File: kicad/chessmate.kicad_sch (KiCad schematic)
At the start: 37 parts, among them J1 SPKR, Q1 2N2222, Q2 2N2222, Q3 2N2222, Q4 2N2222, Q5 2N2222, SW1 F6, SW10 ENTER, SW11 CLEAR, SW12 H8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

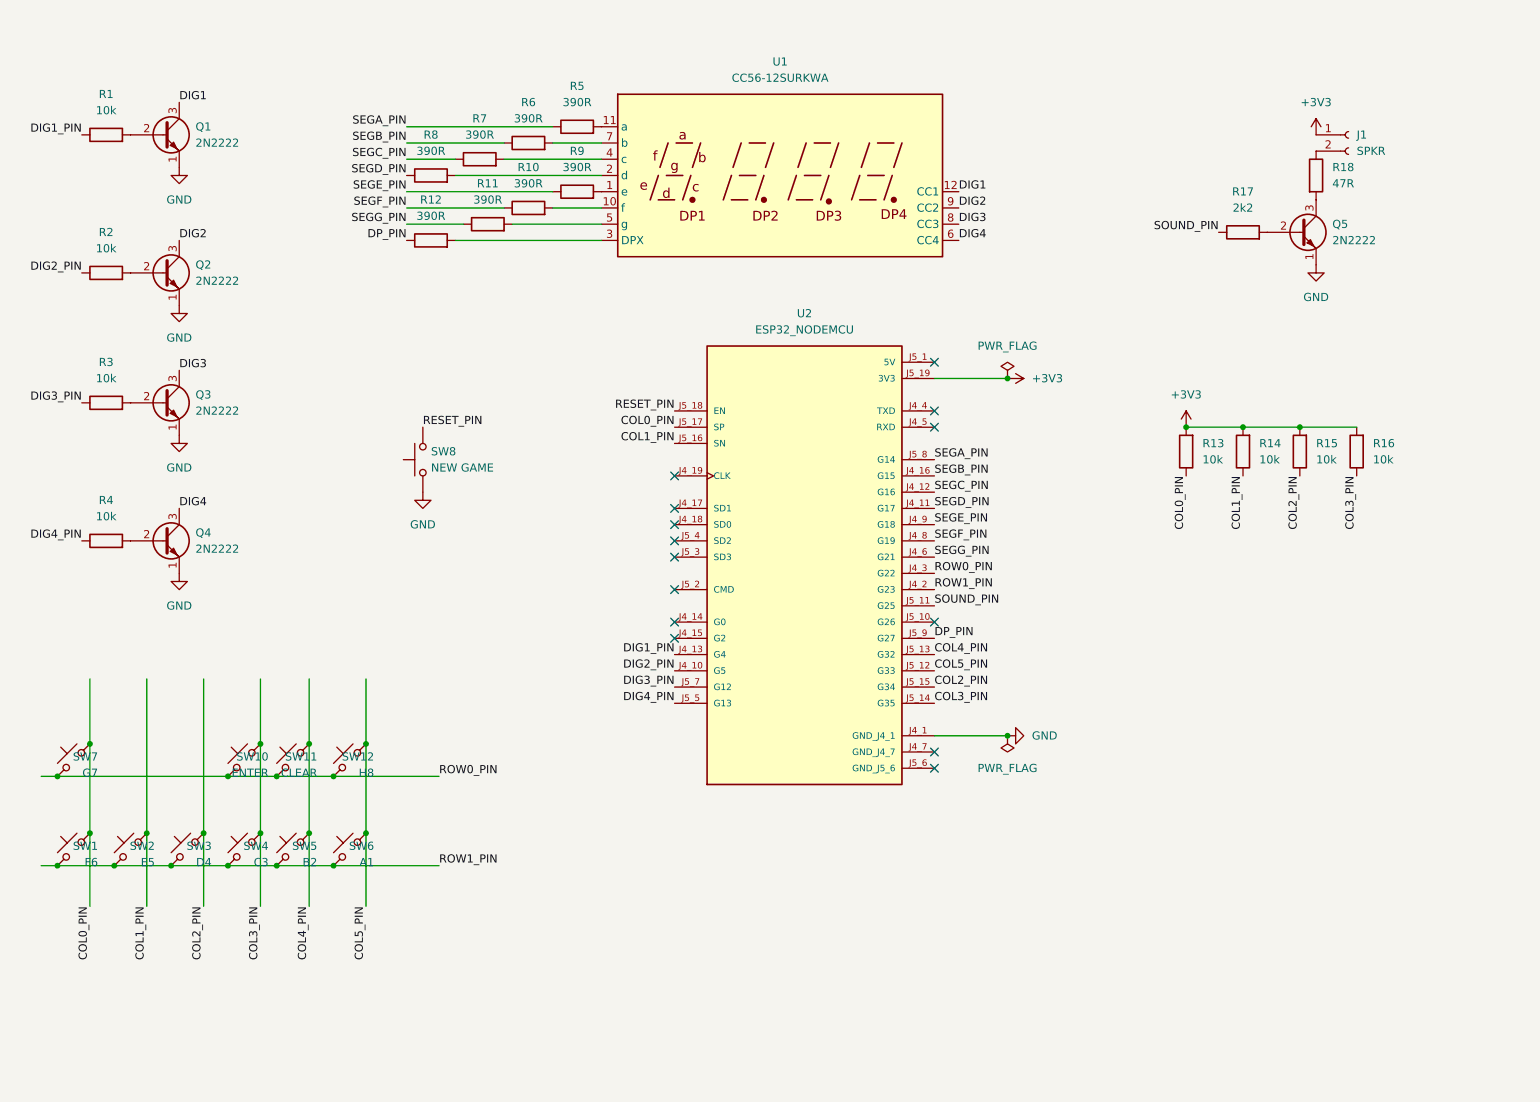
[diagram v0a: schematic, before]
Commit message: add schematic + layout
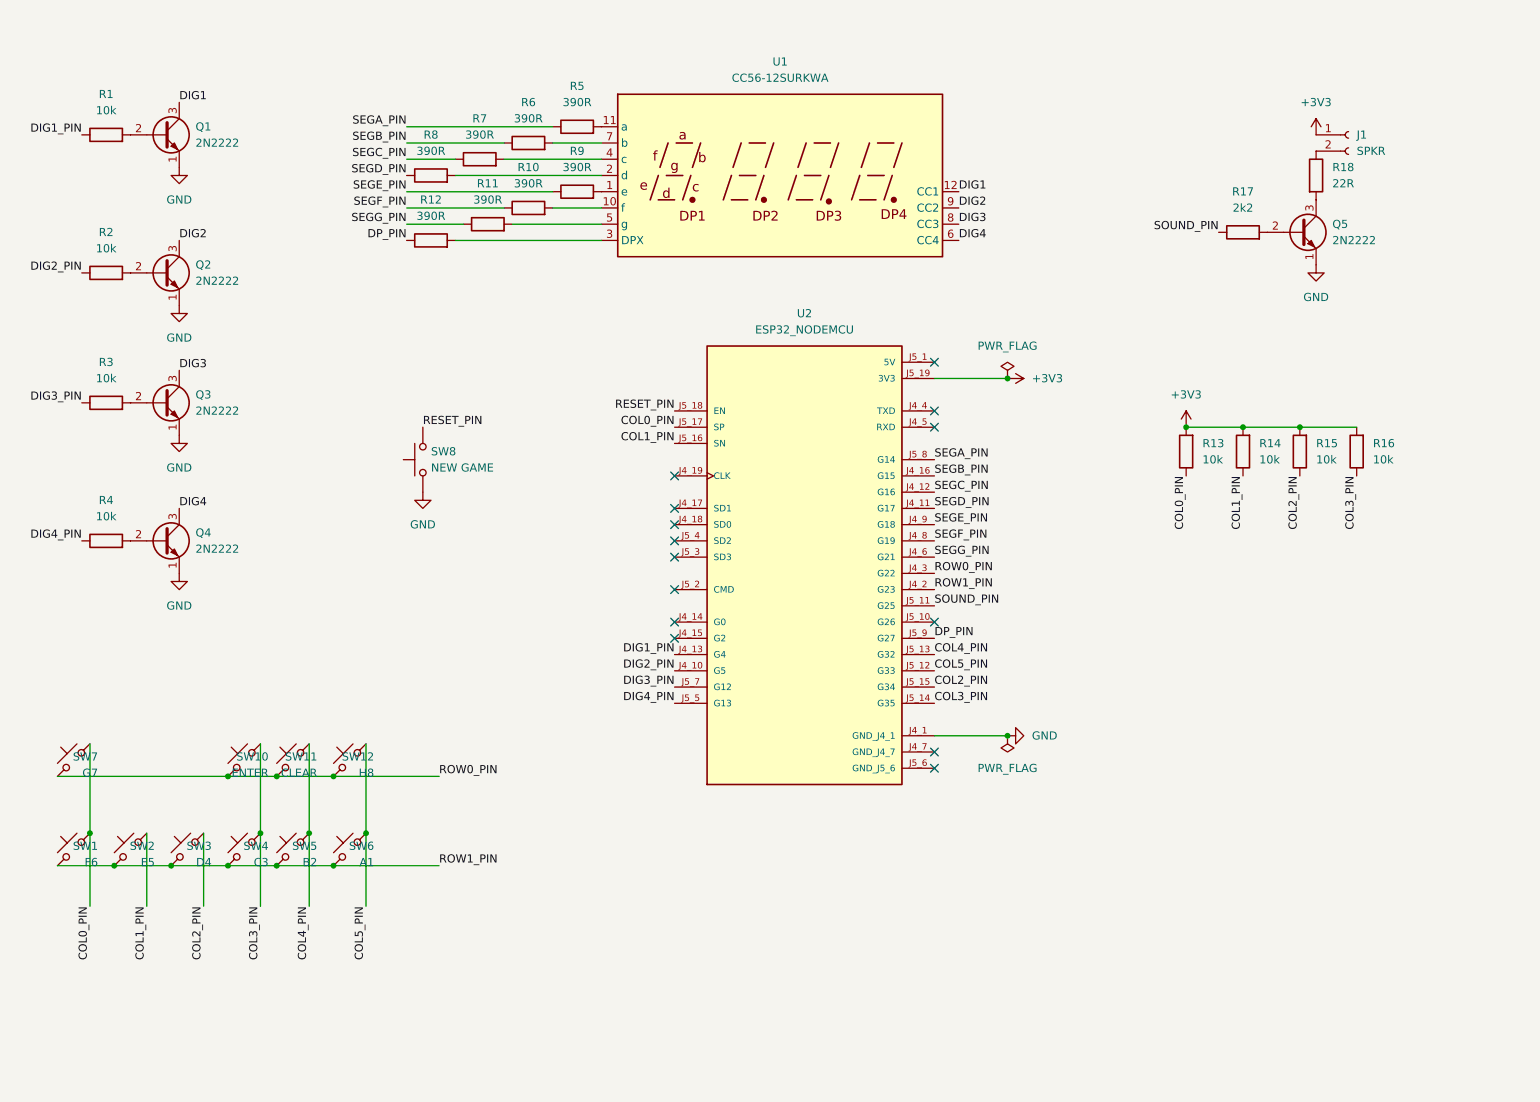
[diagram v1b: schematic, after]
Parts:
- J1: footprint (none) -> Connector_PinHeader_2.54mm:PinHeader_1x02_P2.54mm_Horizontal
- R1, R10, R11, R12, R17, R2, R3, R4, R5, R6, R7, R8, R9: footprint (none) -> Resistor_THT:R_Axial_DIN0207_L6.3mm_D2.5mm_P2.54mm_Vertical
- R13, R14, R15, R16: footprint (none) -> Resistor_THT:R_Axial_DIN0204_L3.6mm_D1.6mm_P5.08mm_Horizontal
- R18: value 47R -> 22R; footprint (none) -> Resistor_THT:R_Axial_DIN0207_L6.3mm_D2.5mm_P2.54mm_Vertical
- SW1, SW10, SW11, SW12, SW2, SW3, SW4, SW5, SW6, SW7, SW8: footprint (none) -> Button_Switch_THT:SW_PUSH_6mm_H4.3mm
- U2: Description_1 NodeMCU is an open source loT platform. ESP32 is a series of low cost, low power system-on-chip (SoC) microcontrollers with integrated Wi-Fi & dual-mode Bluetooth. -> NodeMCU is an open source loT platform. ESP32 is a series of low cost, low power system-on-chip (SoC) microcontrollers with integrated Wi-Fi & dual-mode Bluetooth.

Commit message: kicad updates
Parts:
- removed J1: SPKR, Connector_PinHeader_2.54mm:PinHeader_1x02_P2.54mm_Horizontal, symbol Connector:Conn_01x02_Socket
- added C1: 220uF, Capacitor_THT:CP_Radial_D6.3mm_P2.50mm, symbol Device:C_Polarized
- added D1: 1N4148, Diode_THT:D_DO-35_SOD27_P7.62mm_Horizontal, symbol Diode:1N4148
- added J2: Power Jack, Connector_BarrelJack:BarrelJack_Horizontal, symbol Connector:Barrel_Jack_Switch
- added LS1: Speaker, Buzzer_Beeper:Buzzer_12x9.5RM7.6, symbol Device:Speaker
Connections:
- net GND: now also C1.2, J2.2, J2.3
- net +5V: now reaches U2.J5_1 (5V)
- net +5V: now also R18.1, C1.1, J2.1
- net at R18.2: now also D1.1 (K), LS1.1; no longer Q5.3 (C)
- new net: D1.2 (A), LS1.2, Q5.3 (C)
- no-connect marks 14 -> 13
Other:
- moved on the sheet: R18

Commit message: Address v1.0 PCB errors (#13)
* replace 7-seg footprint with pin headers
* update nodemcu footprint
* move component values and switch names to F.Silkscreen layer
* routing
* add ground plane
* add mounting holes
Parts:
- removed U1: CC56-12SURKWA, Display_7Segment:CA56-12SURKWA, symbol Display_Character:CC56-12SURKWA
- removed U2: ESP32_NODEMCU, ESP32_NODEMCU:MODULE_ESP32_NODEMCU, symbol ESP32_NODEMCU:ESP32_NODEMCU
- added J1: 7SegBtm, Connector_PinHeader_2.54mm:PinHeader_1x06_P2.54mm_Vertical, symbol Connector:Conn_01x06_Socket
- added J3: 7SegTop, Connector_PinHeader_2.54mm:PinHeader_1x06_P2.54mm_Vertical, symbol Connector:Conn_01x06_Socket
- added U1: AI-Thinker Nodemcu-32S, kicad-nodemcu32S-main:ai-thinker nodemcu-32s, symbol ai-thinker nodemcu-32s:AI-Thinker Nodemcu-32S
- LS1: footprint Buzzer_Beeper:Buzzer_12x9.5RM7.6 -> stevelib:Buzzer_12x9.5RM7.0
- R13, R14, R15, R16: footprint Resistor_THT:R_Axial_DIN0204_L3.6mm_D1.6mm_P5.08mm_Horizontal -> Resistor_THT:R_Axial_DIN0207_L6.3mm_D2.5mm_P7.62mm_Horizontal
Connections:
- net +3V3: now also U1.1 (3.3V)
- net +5V: now also U1.19 (5V)
- net COL0_PIN: now also U1.3 (GPI36)
- net COL1_PIN: now also U1.4 (GPI39)
- net COL2_PIN: now also U1.5 (GPI34)
- net COL3_PIN: now also U1.6 (GPI35)
- net COL4_PIN: now also U1.7 (GPIO32)
- net COL5_PIN: now also U1.8 (GPIO33)
- net DIG1_PIN: now also U1.26 (GPIO4)
- net DIG2_PIN: now also U1.29 (GPIO5)
- net DIG3_PIN: now also U1.13 (GPIO12)
- net DIG4_PIN: now also U1.15 (GPIO13)
- net DP_PIN: now also U1.11 (GPIO27)
- net GND: now also U1.14 (GND), U1.38 (GND)
- net RESET_PIN: now also U1.2 (EN_RST)
- net ROW0_PIN: now also U1.36 (GPIO22)
- net ROW1_PIN: now also U1.37 (GPIO23)
- net SEGA_PIN: now also U1.12 (GPIO14)
- net SEGB_PIN: now also U1.23 (GPIO15)
- net SEGC_PIN: now also U1.27 (GPIO16)
- net SEGD_PIN: now also U1.28 (GPIO17)
- net SEGE_PIN: now also U1.30 (GPIO18)
- net SEGF_PIN: now also U1.31 (GPIO19)
- net SEGG_PIN: now also U1.33 (GPIO21)
- net SOUND_PIN: now also U1.9 (GPIO25)
- net C: now reaches R7.2
- net C: now also J1.4 (Pin_4)
- net B: now reaches R6.2
- net B: now also J3.6 (Pin_6)
- net F: now reaches R10.2
- net F: now also J3.3 (Pin_3)
- net A: now reaches R5.2
- net A: now also J3.2 (Pin_2)
- net DP: now reaches R12.2
- net DP: now also J1.3 (Pin_3)
- net G: now reaches R11.2
- net G: now also J1.5 (Pin_5)
- net E: now reaches R9.2
- net E: now also J1.1 (Pin_1)
- net D: now reaches R8.2
- net D: now also J1.2 (Pin_2)
- net DIG1 renamed D1
- net D1: now also J3.1 (Pin_1)
- net DIG2 renamed D2
- net D2: now also J3.4 (Pin_4)
- net DIG3 renamed D3
- net D3: now also J3.5 (Pin_5)
- net DIG4 renamed D4
- net D4: now also J1.6 (Pin_6)
- no-connect marks 13 -> 11
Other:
- moved on the sheet: C1, D1, J2, LS1, Q5, R13, R14, R15, R16, R17, R18, SW1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
